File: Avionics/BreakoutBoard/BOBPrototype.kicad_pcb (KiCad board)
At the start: 2 copper layers, 11 parts

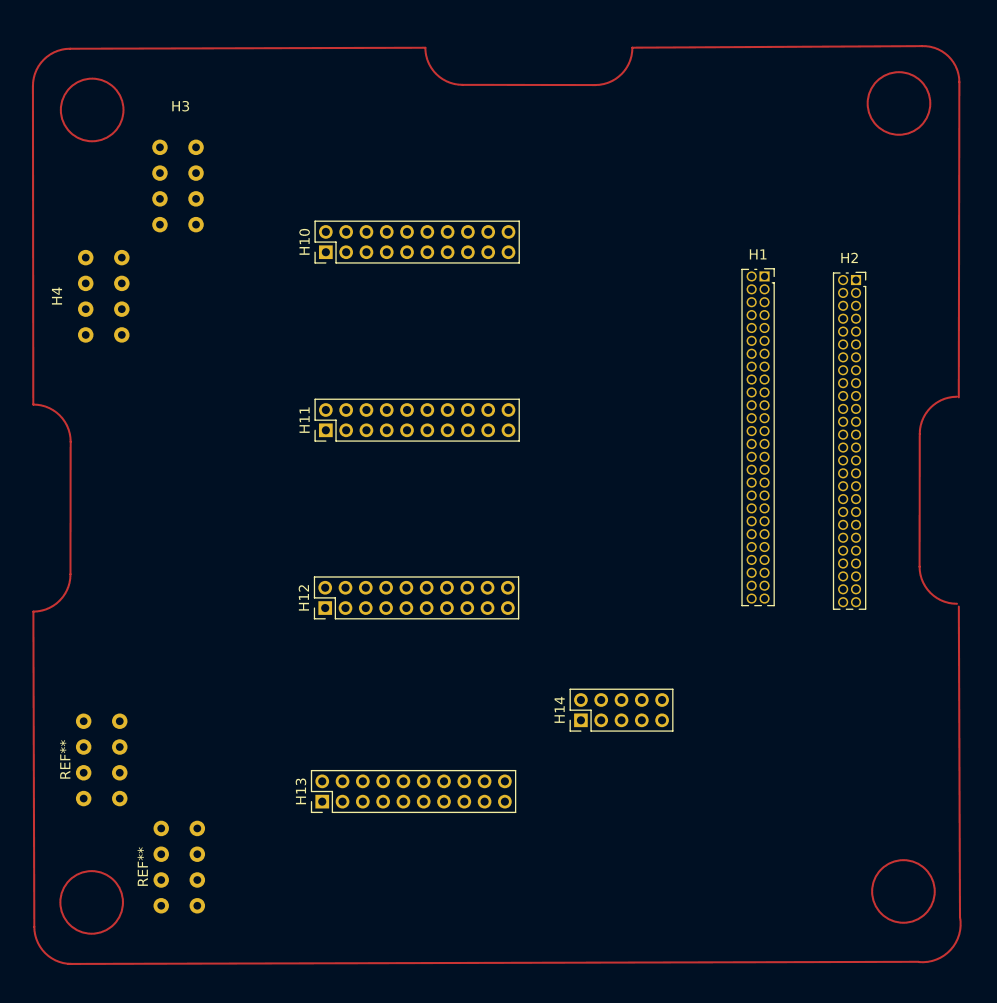
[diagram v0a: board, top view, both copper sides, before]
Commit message: Sephora Poteau: Added changes to schema and pcb
Added 3V3 voltage indicator for power recieved by PCB and BOB has been appropriately traced and filled with copper
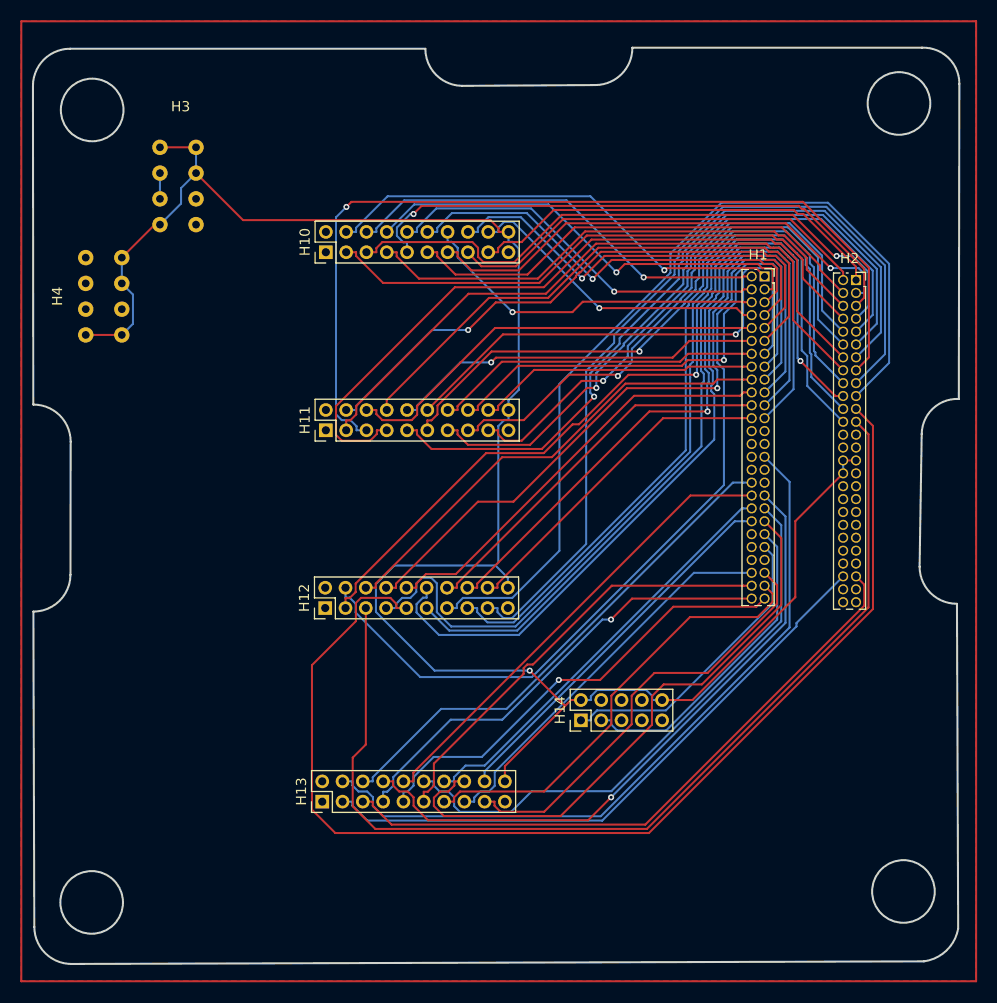
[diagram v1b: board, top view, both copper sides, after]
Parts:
- removed REF** (x2): 8Tholes, Library:8Tholes
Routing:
- net GND: track 0.00 -> 193.4 mm, vias 0 -> 1
- net Net-(H12-Pin_9): track 0.00 -> 113.8 mm
- net Net-(H12-Pin_5): track 0.00 -> 99.7 mm
- net Net-(H12-Pin_7): track 0.00 -> 90.3 mm
- net Net-(H11-Pin_5): track 0.00 -> 89.8 mm, vias 0 -> 1
- net Net-(H1-P3.7): track 0.00 -> 89.1 mm
- net Net-(H12-Pin_13): track 0.00 -> 88.0 mm
- net Net-(H12-Pin_3): track 0.00 -> 85.1 mm, vias 0 -> 1
- net Net-(H12-Pin_17): track 0.00 -> 83.4 mm
- net Net-(H1-P3.3): track 0.00 -> 81.7 mm
- net Net-(H12-Pin_11): track 0.00 -> 79.5 mm, vias 0 -> 1
- net Net-(H12-Pin_15): track 0.00 -> 75.4 mm
- net Net-(H1-P3.5): track 0.00 -> 73.4 mm, vias 0 -> 1
- net Net-(H11-Pin_7): track 0.00 -> 73.3 mm
- net Net-(H11-Pin_9): track 0.00 -> 73.1 mm, vias 0 -> 1
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- added copper zone on B.Cu, net GND
- added copper zone on F.Cu, net GND
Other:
- board outline added: 91.3 x 90.3 mm
